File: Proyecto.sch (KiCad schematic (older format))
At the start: 52 parts, among them P1 CONN_01X03, P2 CONN_01X03, Q1 BC808-40, Q2 BC808-40, U1 MCP2515, U2 MCP2551-I/SN, U3 AMS1117, U4 ACS712, U5 ACS712

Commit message: fix tamaños y nuevas librerias
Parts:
- C10, C11, C3, C4, C6, C7, C8, C9, CFilter1, CFliter1: footprint Capacitors_ThroughHole:C_Disc_D3_P2.5 -> w_capacitors:cnp_6mm_disc
- CAN1, S0: footprint Terminal_Blocks:TerminalBlock_Pheonix_MPT-2.54mm_2pol -> w_conn_mkds:mkds_1,5-2
- Crystal2: footprint Crystals:Crystal_HC49-U_Vertical -> w_crystal:crystal_hc-49s
- D_RX1, D_TX1, LED1, LED_Gp1, LED_Gp2, LED_Vcc1: footprint LEDs:LED-5MM -> LEDs:LED-3MM
- ESP8266: footprint Pin_Headers:Pin_Header_Straight_2x04 -> w_pin_strip:pin_socket_4x2
- P1, P2: footprint Terminal_Blocks:TerminalBlock_Pheonix_MPT-2.54mm_3pol -> w_conn_mkds:mkds_1,5-3
- PIN_L1, PIN_R1: footprint Pin_Headers:Pin_Header_Straight_1x15 -> w_pin_strip:pin_socket_2mm_15
- R1, R10, R11, R12, R13, R2, R3, R4, R5, R6, R7, R8, R9: footprint Resistors_ThroughHole:Resistor_Horizontal_RM10mm -> w_pth_resistors:RC05
- U3: symbol AMS1117 -> AMS1117-RESCUE-Proyecto
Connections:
- net labels added: PIN23, PIN24
- net labels removed: pin23, pin24
- wire segments 200 -> 198

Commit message: fix pcb casa
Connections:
- wire segments 198 -> 200
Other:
- moved on the sheet: LED_Gp1, LED_Gp2, R6, R7
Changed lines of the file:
@@
 LIBS:mylib
 LIBS:HK4100F
-LIBS:acs712
-LIBS:AMS1117
 LIBS:Proyecto-cache
 EELAYER 25 0
@@
 L LED LED_Gp2
 U 1 1 5777088E
+P 1600 3000
+F 0 "LED_Gp2" H 1600 3100 50  0000 C CIN
+F 1 "LED" H 1600 2900 50  0000 C CNN
+F 2 "LEDs:LED-3MM" H 1600 3000 50  0001 C CNN
+F 3 "" H 1600 3000 50  0000 C CNN
+	1    1600 3000
+	0    -1   -1   0
+$EndComp
+$Comp
+L R R6
+U 1 1 57770894
 P 1600 2600
-F 0 "LED_Gp2" H 1600 2700 50  0000 C CIN
-F 1 "LED" H 1600 2500 50  0000 C CNN
-F 2 "LEDs:LED-3MM" H 1600 2600 50  0001 C CNN
+F 0 "R6" V 1680 2600 50  0000 C CNN
+F 1 "1k" V 1600 2600 50  0000 C CNN
+F 2 "w_pth_resistors:RC05" V 1530 2600 50  0001 C CNN
 F 3 "" H 1600 2600 50  0000 C CNN
 	1    1600 2600
-	0    -1   -1   0
-$EndComp
-$Comp
-L R R6
-U 1 1 57770894
-P 1600 3000
-F 0 "R6" V 1680 3000 50  0000 C CNN
-F 1 "1k" V 1600 3000 50  0000 C CNN
-F 2 "w_pth_resistors:RC05" V 1530 3000 50  0001 C CNN
-F 3 "" H 1600 3000 50  0000 C CNN
-	1    1600 3000
 	1    0    0    -1
 $EndComp
@@
 L GND-RESCUE-Proyecto #PWR033
 U 1 1 5777089A
-P 1600 3200
-F 0 "#PWR033" H 1600 2950 50  0001 C CNN
-F 1 "GND" H 1600 3050 50  0000 C CNN
-F 2 "" H 1600 3200 50  0000 C CNN
-F 3 "" H 1600 3200 50  0000 C CNN
-	1    1600 3200
+P 1600 3250
+F 0 "#PWR033" H 1600 3000 50  0001 C CNN
+F 1 "GND" H 1600 3100 50  0000 C CNN
+F 2 "" H 1600 3250 50  0000 C CNN
+F 3 "" H 1600 3250 50  0000 C CNN
+	1    1600 3250
 	1    0    0    -1
 $EndComp
 Wire Wire Line
 	1450 2400 1600 2400
-Wire Wire Line
-	1600 2800 1600 2850
-Wire Wire Line
-	1600 3150 1600 3200
 Wire Wire Line
 	2950 6600 2850 6600
@@
 L LED LED_Gp1
 U 1 1 57770BB7
+P 1900 3000
+F 0 "LED_Gp1" H 1900 3100 50  0000 C CIN
+F 1 "LED" H 1900 2900 50  0000 C CNN
+F 2 "LEDs:LED-3MM" H 1900 3000 50  0001 C CNN
+F 3 "" H 1900 3000 50  0000 C CNN
+	1    1900 3000
+	0    -1   -1   0
+$EndComp
+$Comp
+L R R7
+U 1 1 57770BBD
 P 1900 2600
-F 0 "LED_Gp1" H 1900 2700 50  0000 C CIN
-F 1 "LED" H 1900 2500 50  0000 C CNN
-F 2 "LEDs:LED-3MM" H 1900 2600 50  0001 C CNN
+F 0 "R7" V 1980 2600 50  0000 C CNN
+F 1 "1k" V 1900 2600 50  0000 C CNN
+F 2 "w_pth_resistors:RC05" V 1830 2600 50  0001 C CNN
 F 3 "" H 1900 2600 50  0000 C CNN
 	1    1900 2600
-	0    -1   -1   0
-$EndComp
-$Comp
-L R R7
-U 1 1 57770BBD
-P 1900 3000
-F 0 "R7" V 1980 3000 50  0000 C CNN
-F 1 "1k" V 1900 3000 50  0000 C CNN
-F 2 "w_pth_resistors:RC05" V 1830 3000 50  0001 C CNN
-F 3 "" H 1900 3000 50  0000 C CNN
-	1    1900 3000
 	1    0    0    -1
 $EndComp
@@
 L GND-RESCUE-Proyecto #PWR034
 U 1 1 57770BC3
-P 1900 3200
-F 0 "#PWR034" H 1900 2950 50  0001 C CNN
-F 1 "GND" H 1900 3050 50  0000 C CNN
-F 2 "" H 1900 3200 50  0000 C CNN
-F 3 "" H 1900 3200 50  0000 C CNN
-	1    1900 3200
+P 1900 3250
+F 0 "#PWR034" H 1900 3000 50  0001 C CNN
+F 1 "GND" H 1900 3100 50  0000 C CNN
+F 2 "" H 1900 3250 50  0000 C CNN
+F 3 "" H 1900 3250 50  0000 C CNN
+	1    1900 3250
 	1    0    0    -1
 $EndComp
 Wire Wire Line
 	1750 2400 1900 2400
-Wire Wire Line
-	1900 2800 1900 2850
-Wire Wire Line
-	1900 3150 1900 3200
 Text Label 1450 2400 0    60   ~ 0
 Gp2
@@
 Text Label 2050 2400 0    60   ~ 0
 Vcc
-Wire Wire Line
-	1300 3150 1300 3250
 Wire Wire Line
 	5700 2300 6000 2300
@@
 Wire Wire Line
 	8150 3300 8150 3250
+Wire Wire Line
+	1300 3150 1300 3250
+Wire Wire Line
+	1900 3250 1900 3200
+Wire Wire Line
+	1600 3250 1600 3200
+Wire Wire Line
+	1900 2800 1900 2750
+Wire Wire Line
+	1600 2800 1600 2750
+Wire Wire Line
+	1600 2400 1600 2450
+Wire Wire Line
+	1900 2400 1900 2450
 $EndSCHEMATC

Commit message: fisx
con 4 puentes... 6.6 cm x12 cm
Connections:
- wire segments 200 -> 199
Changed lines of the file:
@@
 LIBS:mylib
 LIBS:HK4100F
+LIBS:acs712
+LIBS:AMS1117
 LIBS:Proyecto-cache
 EELAYER 25 0
@@
 	3450 6250 3450 6300
 Wire Wire Line
-	3450 6300 3750 6300
-Wire Wire Line
 	3600 6300 3600 6400
 Connection ~ 3600 6300
@@
 	7950 2750 7950 2950
 Wire Wire Line
-	4800 5950 4800 6950
-Wire Wire Line
 	4950 6650 4950 6750
 Wire Wire Line
@@
 Wire Wire Line
 	8300 5450 8300 5750
-Wire Wire Line
-	4800 6950 4950 6950
 Connection ~ 4950 6950
 Wire Wire Line
-	4950 6700 4600 6700
-Wire Wire Line
-	4600 6700 4600 6950
-Wire Wire Line
-	4600 6950 4400 6950
+	4400 6950 4950 6950
 Connection ~ 4950 6700
 Connection ~ 8400 5100
@@
 	2050 1750 2050 1650
 Wire Wire Line
-	3450 5900 3750 5900
-Wire Wire Line
-	3750 5900 3750 6050
-Wire Wire Line
-	3750 6300 3750 6150
-Wire Wire Line
-	3600 5850 3600 5900
+	3600 5850 3600 6150
 Connection ~ 3600 5900
 Wire Wire Line
@@
 Wire Wire Line
 	1900 2400 1900 2450
+Wire Wire Line
+	3450 5900 3600 5900
+Wire Wire Line
+	3450 6300 3700 6300
+Wire Wire Line
+	3600 6150 3750 6150
+Wire Wire Line
+	3750 6050 3700 6050
+Wire Wire Line
+	3700 6050 3700 6300
+Wire Wire Line
+	4950 6700 4800 6700
+Wire Wire Line
+	4800 6700 4800 5950
 $EndSCHEMATC

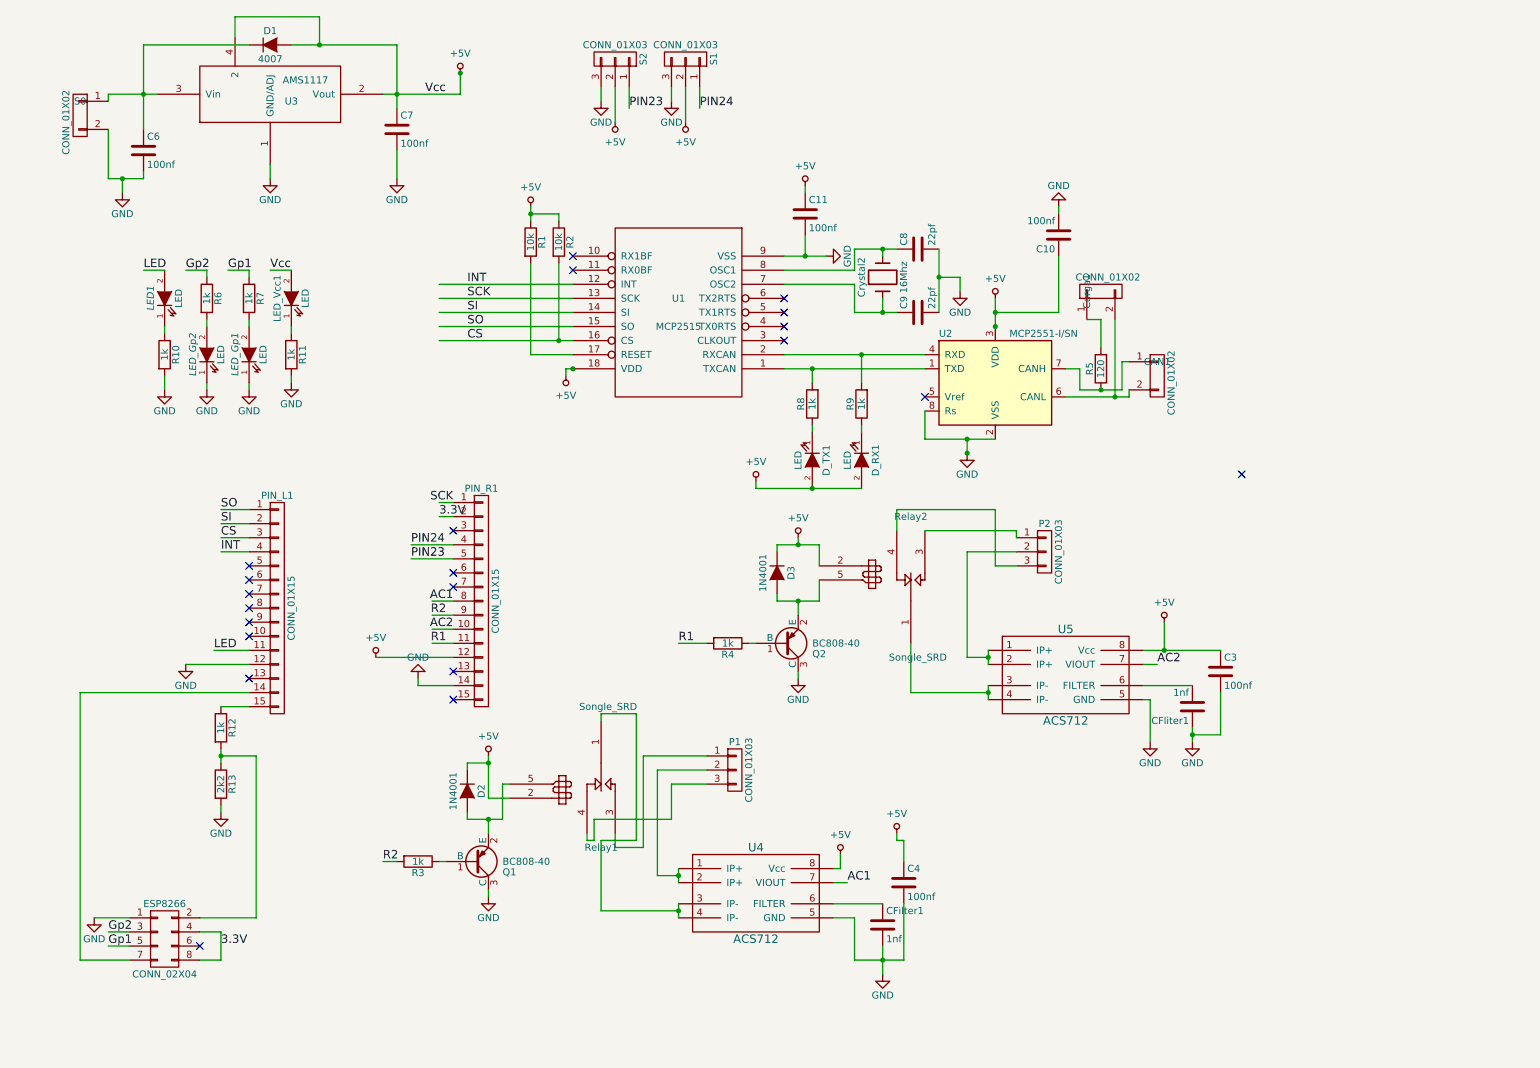
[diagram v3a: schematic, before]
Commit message: fix
achicamiento 6.5 x 10.7 cm
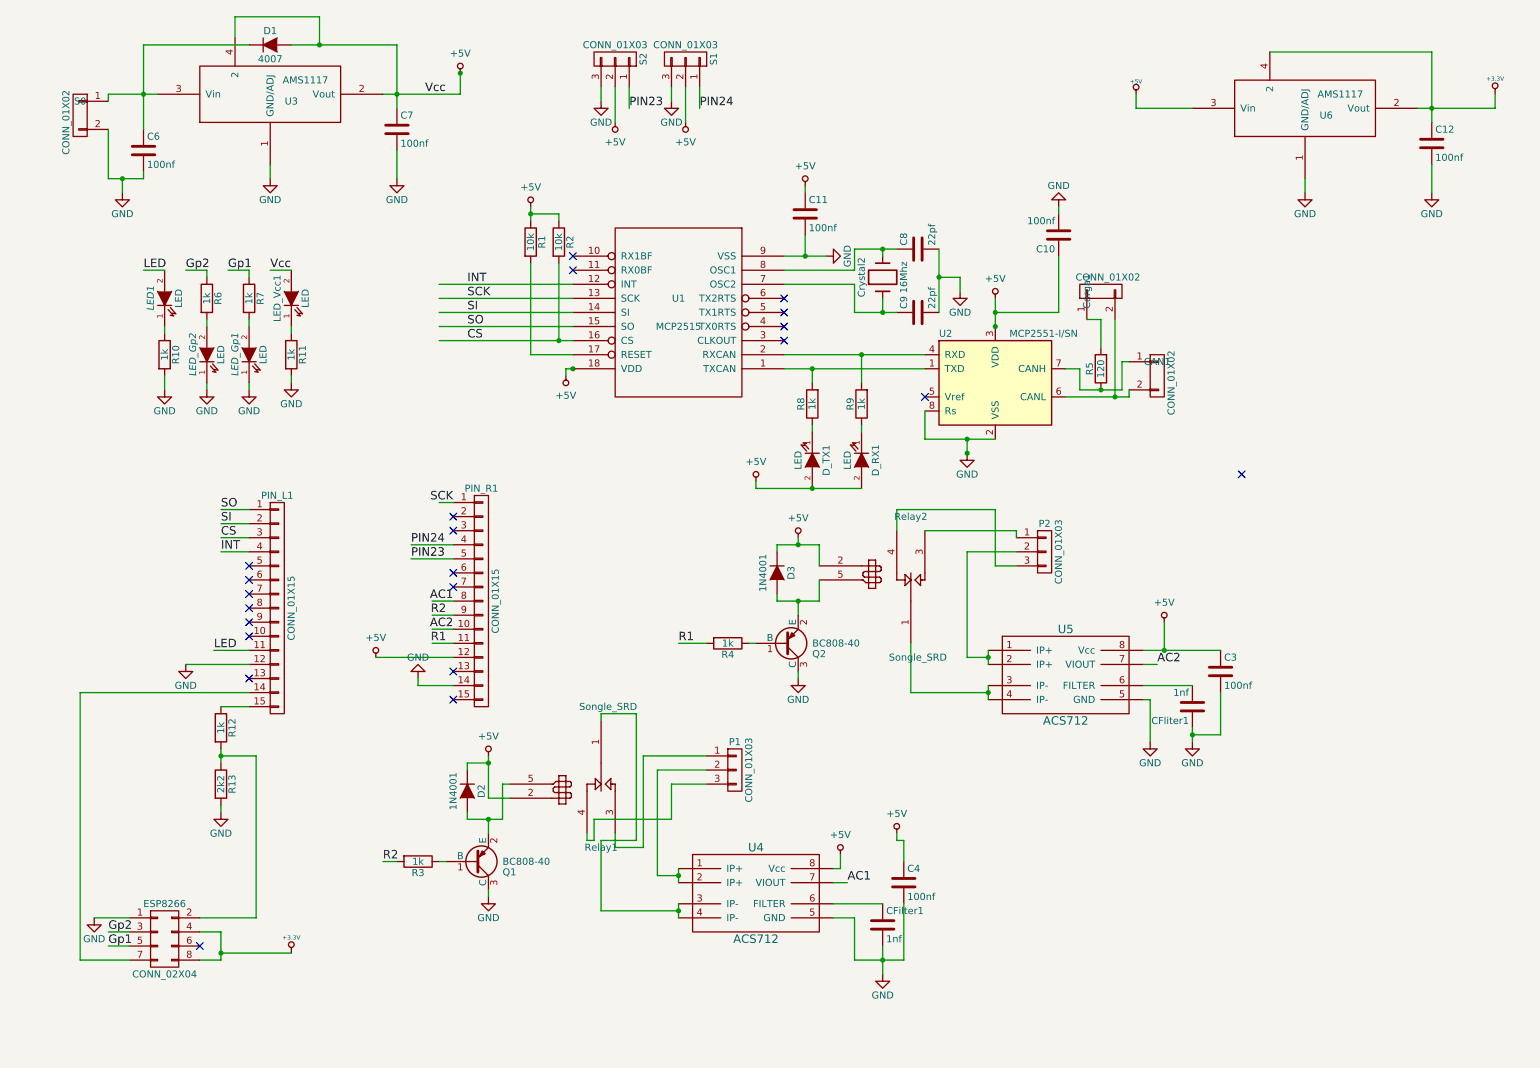
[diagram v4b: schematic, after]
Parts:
- added C12: 100nf, w_capacitors:cnp_6mm_disc, symbol C
- added U6: AMS1117, TO_SOT_Packages_SMD:SOT-223, symbol AMS1117-RESCUE-Proyecto
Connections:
- net labels added: +3.3V
- net labels removed: 3.3V
- wire segments 199 -> 207
- no-connect marks 21 -> 22
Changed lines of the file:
@@
 LIBS:mylib
 LIBS:HK4100F
-LIBS:acs712
-LIBS:AMS1117
 LIBS:Proyecto-cache
 EELAYER 25 0
@@
 Wire Wire Line
 	1700 7300 1550 7300
-Text Label 1700 7200 0    60   ~ 0
-3.3V
-Wire Wire Line
-	3350 4150 3250 4150
-Text Label 3250 4150 0    60   ~ 0
-3.3V
 $Comp
 L R R13
@@
 Wire Wire Line
 	4800 6700 4800 5950
+$Comp
+L AMS1117-RESCUE-Proyecto U6
+U 1 1 577DDDC7
+P 9400 1250
+F 0 "U6" H 9550 1200 50  0000 C CNN
+F 1 "AMS1117" H 9650 1350 50  0000 C CNN
+F 2 "TO_SOT_Packages_SMD:SOT-223" H 9400 1250 60  0001 C CNN
+F 3 "" H 9400 1250 60  0000 C CNN
+	1    9400 1250
+	1    0    0    -1
+$EndComp
+$Comp
+L GND-RESCUE-Proyecto #PWR037
+U 1 1 577DDDCD
+P 9400 1850
+F 0 "#PWR037" H 9400 1600 50  0001 C CNN
+F 1 "GND" H 9400 1700 50  0000 C CNN
+F 2 "" H 9400 1850 50  0000 C CNN
+F 3 "" H 9400 1850 50  0000 C CNN
+	1    9400 1850
+	1    0    0    -1
+$EndComp
+$Comp
+L C C12
+U 1 1 577DDDD3
+P 10300 1500
+F 0 "C12" H 10325 1600 50  0000 L CNN
+F 1 "100nf" H 10325 1400 50  0000 L CNN
+F 2 "w_capacitors:cnp_6mm_disc" H 10338 1350 50  0001 C CNN
+F 3 "" H 10300 1500 50  0000 C CNN
+	1    10300 1500
+	1    0    0    -1
+$EndComp
+$Comp
+L GND-RESCUE-Proyecto #PWR038
+U 1 1 577DDDDF
+P 10300 1850
+F 0 "#PWR038" H 10300 1600 50  0001 C CNN
+F 1 "GND" H 10300 1700 50  0000 C CNN
+F 2 "" H 10300 1850 50  0000 C CNN
+F 3 "" H 10300 1850 50  0000 C CNN
+	1    10300 1850
+	1    0    0    -1
+$EndComp
+Wire Wire Line
+	8200 1250 8600 1250
+Wire Wire Line
+	10200 1250 10750 1250
+Connection ~ 10300 1250
+Wire Wire Line
+	9400 1850 9400 1750
+Wire Wire Line
+	10300 1650 10300 1850
+Wire Wire Line
+	10300 850  10300 1350
+Wire Wire Line
+	9150 850  10300 850
+$Comp
+L +3.3V #PWR039
+U 1 1 577DE689
+P 10750 1150
+F 0 "#PWR039" H 10750 1110 30  0001 C CNN
+F 1 "+3.3V" H 10750 1260 30  0000 C CNN
+F 2 "" H 10750 1150 60  0000 C CNN
+F 3 "" H 10750 1150 60  0000 C CNN
+	1    10750 1150
+	1    0    0    -1
+$EndComp
+Wire Wire Line
+	10750 1250 10750 1150
+$Comp
+L +5V #PWR040
+U 1 1 577DEE88
+P 8200 1150
+F 0 "#PWR040" H 8200 1240 20  0001 C CNN
+F 1 "+5V" H 8200 1240 30  0000 C CNN
+F 2 "" H 8200 1150 60  0000 C CNN
+F 3 "" H 8200 1150 60  0000 C CNN
+	1    8200 1150
+	1    0    0    -1
+$EndComp
+Wire Wire Line
+	8200 1150 8200 1250
+$Comp
+L +3.3V #PWR041
+U 1 1 577DD92E
+P 2200 7250
+F 0 "#PWR041" H 2200 7210 30  0001 C CNN
+F 1 "+3.3V" H 2200 7360 30  0000 C CNN
+F 2 "" H 2200 7250 60  0000 C CNN
+F 3 "" H 2200 7250 60  0000 C CNN
+	1    2200 7250
+	1    0    0    -1
+$EndComp
+Wire Wire Line
+	2200 7250 1700 7250
+Connection ~ 1700 7250
+NoConn ~ 3350 4150
 $EndSCHEMATC

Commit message: casa
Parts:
- added S3, S4: CONN_01X03, Pin_Headers:Pin_Header_Straight_1x03, symbol CONN_01X03
- PIN_L1, PIN_R1: footprint w_pin_strip:pin_socket_2mm_15 -> w_pin_strip:pin_socket_15
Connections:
- net labels added: PIN25, PIN26
- wire segments 207 -> 218
- no-connect marks 22 -> 20
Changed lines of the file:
@@
 F 0 "PIN_R1" H 3550 5550 50  0000 C CNN
 F 1 "CONN_01X15" V 3650 4750 50  0000 C CNN
-F 2 "w_pin_strip:pin_socket_2mm_15" H 3550 4750 50  0001 C CNN
+F 2 "w_pin_strip:pin_socket_15" H 3550 4750 50  0001 C CNN
 F 3 "" H 3550 4750 50  0000 C CNN
 	1    3550 4750
@@
 F 0 "PIN_L1" H 2100 5600 50  0000 C CNN
 F 1 "CONN_01X15" V 2200 4800 50  0000 C CNN
-F 2 "w_pin_strip:pin_socket_2mm_15" H 2100 4800 50  0001 C CNN
+F 2 "w_pin_strip:pin_socket_15" H 2100 4800 50  0001 C CNN
 F 3 "" H 2100 4800 50  0000 C CNN
 	1    2100 4800
@@
 $EndComp
 NoConn ~ 3350 5250
-NoConn ~ 3350 4650
-NoConn ~ 3350 4550
 NoConn ~ 3350 4250
 Text Label 6150 6750 0    60   ~ 0
@@
 Connection ~ 1700 7250
 NoConn ~ 3350 4150
+$Comp
+L PWR_FLAG #FLG042
+U 1 1 57840DBD
+P 950 1100
+F 0 "#FLG042" H 950 1370 30  0001 C CNN
+F 1 "PWR_FLAG" H 950 1330 30  0000 C CNN
+F 2 "" H 950 1100 60  0000 C CNN
+F 3 "" H 950 1100 60  0000 C CNN
+	1    950  1100
+	1    0    0    -1
+$EndComp
+Wire Wire Line
+	950  1100 950  1150
+Connection ~ 950  1150
+$Comp
+L PWR_FLAG #FLG043
+U 1 1 57841CE9
+P 700 1750
+F 0 "#FLG043" H 700 2020 30  0001 C CNN
+F 1 "PWR_FLAG" H 700 1980 30  0000 C CNN
+F 2 "" H 700 1750 60  0000 C CNN
+F 3 "" H 700 1750 60  0000 C CNN
+	1    700  1750
+	-1   0    0    1
+$EndComp
+Wire Wire Line
+	700  1750 700  1650
+Wire Wire Line
+	700  1650 900  1650
+Connection ~ 900  1650
+$Comp
+L CONN_01X03 S3
+U 1 1 57841E7A
+P 5650 900
+F 0 "S3" H 5650 1100 50  0000 C CNN
+F 1 "CONN_01X03" V 5750 900 50  0000 C CNN
+F 2 "Pin_Headers:Pin_Header_Straight_1x03" H 5650 900 50  0001 C CNN
+F 3 "" H 5650 900 50  0000 C CNN
+	1    5650 900
+	0    1    -1   0
+$EndComp
+$Comp
+L +5V #PWR044
+U 1 1 57841E80
+P 5650 1350
+F 0 "#PWR044" H 5650 1200 50  0001 C CNN
+F 1 "+5V" H 5650 1490 50  0000 C CNN
+F 2 "" H 5650 1350 50  0000 C CNN
+F 3 "" H 5650 1350 50  0000 C CNN
+	1    5650 1350
+	-1   0    0    1
+$EndComp
+$Comp
+L GND-RESCUE-Proyecto #PWR045
+U 1 1 57841E86
+P 5550 1200
+F 0 "#PWR045" H 5550 950 50  0001 C CNN
+F 1 "GND" H 5550 1050 50  0000 C CNN
+F 2 "" H 5550 1200 50  0000 C CNN
+F 3 "" H 5550 1200 50  0000 C CNN
+	1    5550 1200
+	1    0    0    -1
+$EndComp
+Wire Wire Line
+	5550 1100 5550 1200
+Wire Wire Line
+	5650 1100 5650 1350
+Wire Wire Line
+	5750 1100 5750 1250
+Text Label 5750 1250 0    60   ~ 0
+PIN25
+$Comp
+L CONN_01X03 S4
+U 1 1 57841F1D
+P 6250 900
+F 0 "S4" H 6250 1100 50  0000 C CNN
+F 1 "CONN_01X03" V 6350 900 50  0000 C CNN
+F 2 "Pin_Headers:Pin_Header_Straight_1x03" H 6250 900 50  0001 C CNN
+F 3 "" H 6250 900 50  0000 C CNN
+	1    6250 900
+	0    1    -1   0
+$EndComp
+$Comp
+L +5V #PWR046
+U 1 1 57841F23
+P 6250 1350
+F 0 "#PWR046" H 6250 1200 50  0001 C CNN
+F 1 "+5V" H 6250 1490 50  0000 C CNN
+F 2 "" H 6250 1350 50  0000 C CNN
+F 3 "" H 6250 1350 50  0000 C CNN
+	1    6250 1350
+	-1   0    0    1
+$EndComp
+$Comp
+L GND-RESCUE-Proyecto #PWR047
+U 1 1 57841F29
+P 6150 1200
+F 0 "#PWR047" H 6150 950 50  0001 C CNN
+F 1 "GND" H 6150 1050 50  0000 C CNN
+F 2 "" H 6150 1200 50  0000 C CNN
+F 3 "" H 6150 1200 50  0000 C CNN
+	1    6150 1200
+	1    0    0    -1
+$EndComp
+Wire Wire Line
+	6150 1100 6150 1200
+Wire Wire Line
+	6250 1100 6250 1350
+Wire Wire Line
+	6350 1100 6350 1250
+Text Label 6350 1250 0    60   ~ 0
+PIN26
+Wire Wire Line
+	3350 4550 3050 4550
+Text Label 3050 4550 0    60   ~ 0
+PIN25
+Wire Wire Line
+	3350 4650 3050 4650
+Text Label 3050 4650 0    60   ~ 0
+PIN26
 $EndSCHEMATC

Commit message: fix
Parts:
- added C13, C14: 10uf, w_capacitors:CP_5x11mm, symbol CP
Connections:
- wire segments 218 -> 221
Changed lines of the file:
@@
 LIBS:mylib
 LIBS:HK4100F
+LIBS:acs712
+LIBS:AMS1117
+LIBS:w_analog
+LIBS:w_microcontrollers
+LIBS:w_transistor
+LIBS:w_connectors
+LIBS:w_memory
+LIBS:w_rtx
+LIBS:w_logic
+LIBS:w_opto
+LIBS:w_vacuum
+LIBS:w_device
+LIBS:w_relay
 LIBS:Proyecto-cache
 EELAYER 25 0
@@
 Wire Wire Line
 	6200 7000 6200 7300
-Connection ~ 7000 3700
 Connection ~ 7200 2800
 Wire Wire Line
-	3400 1150 3400 1000
+	3400 1000 3400 1400
 Connection ~ 3400 1000
 Wire Wire Line
@@
 $EndComp
 Wire Wire Line
-	10750 1250 10750 1150
+	10750 1150 10750 1400
 $Comp
 L +5V #PWR040
@@
 Text Label 3050 4650 0    60   ~ 0
 PIN26
+$Comp
+L CP C14
+U 1 1 578699D7
+P 3400 1550
+F 0 "C14" H 3425 1650 50  0000 L CNN
+F 1 "10uf" H 3425 1450 50  0000 L CNN
+F 2 "w_capacitors:CP_5x11mm" H 3438 1400 50  0001 C CNN
+F 3 "" H 3400 1550 50  0000 C CNN
+	1    3400 1550
+	1    0    0    -1
+$EndComp
+$Comp
+L CP C13
+U 1 1 57869F7B
+P 10750 1550
+F 0 "C13" H 10775 1650 50  0000 L CNN
+F 1 "10uf" H 10775 1450 50  0000 L CNN
+F 2 "w_capacitors:CP_5x11mm" H 10788 1400 50  0001 C CNN
+F 3 "" H 10750 1550 50  0000 C CNN
+	1    10750 1550
+	1    0    0    -1
+$EndComp
+Connection ~ 10750 1250
+Wire Wire Line
+	10750 1700 10750 1750
+Wire Wire Line
+	10750 1750 10300 1750
+Connection ~ 10300 1750
+Connection ~ 3400 1150
+Wire Wire Line
+	3400 1700 2950 1700
+Connection ~ 2950 1700
 $EndSCHEMATC
